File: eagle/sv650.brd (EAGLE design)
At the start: 54.2 x 52.1 mm, 21 parts, among them IC1 7805

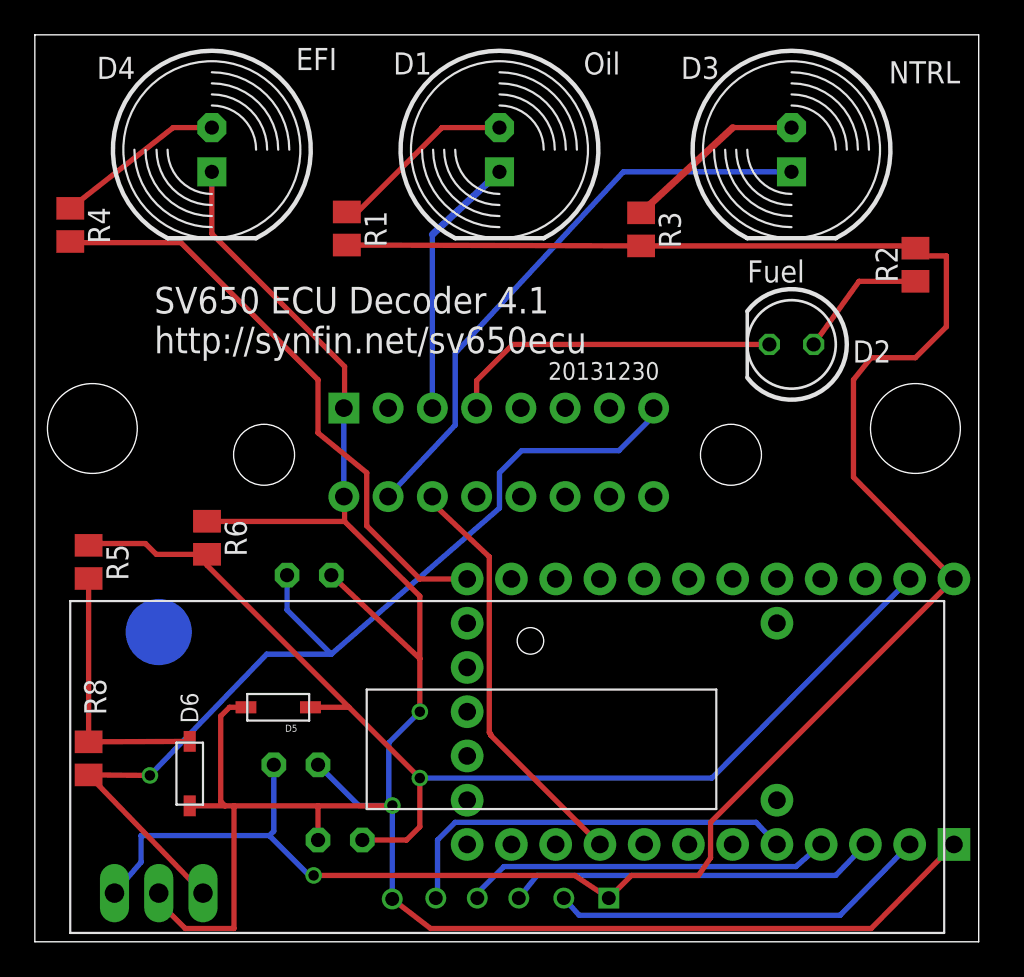
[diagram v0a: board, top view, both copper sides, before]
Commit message: modify the position of parts & traces to be a little cleaner move LED's away from the top edge of the board
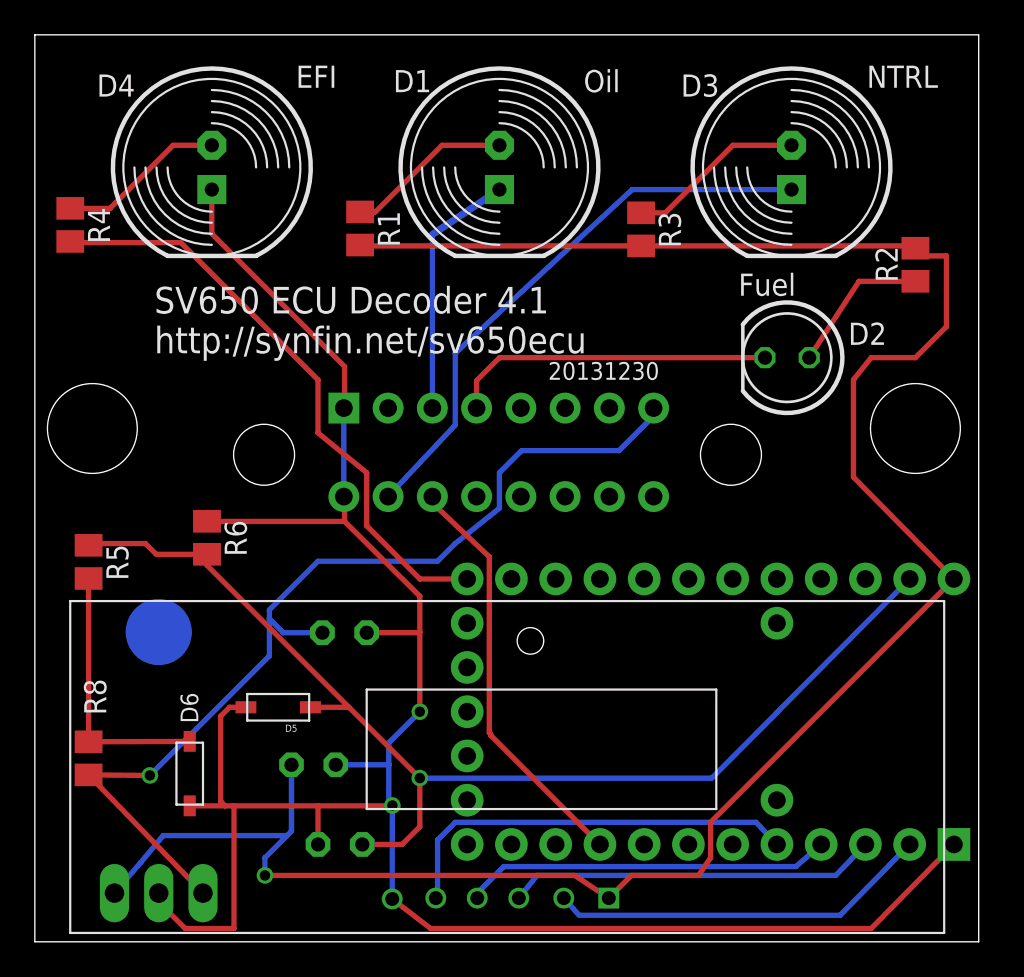
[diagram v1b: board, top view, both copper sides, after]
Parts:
- moved C1 3.88 mm to (17.8, 17.7)
- moved C2 1.02 mm to (16.0, 10.2)
- moved D1 1.02 mm to (26.7, 44.5)
- moved D3 1.02 mm to (43.4, 44.5)
- moved D4 1.02 mm to (10.2, 44.5)
- moved D2 0.80 mm to (43.2, 33.5)
- moved R1 0.76 mm to (18.7, 40.9)
- moved C3 0.25 mm to (17.5, 5.59)
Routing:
- net GND: track 135.6 -> 128.8 mm
- net 5V: track 125.5 -> 127.1 mm
- net N$8: track 10.8 -> 9.73 mm
- net NTRL: track 33.6 -> 32.7 mm
- net N$7: track 7.70 -> 8.47 mm
- net OIL: track 15.2 -> 14.6 mm
- net FUEL: track 19.2 -> 18.7 mm
- net +12V: track 57.4 -> 56.9 mm

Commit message: remove 20V zener replace 5V zener with 4.7V zener (hard to find 5V zeners) merge 10K + 22K into a single 30K resistor clean up traces & remove lots of vias
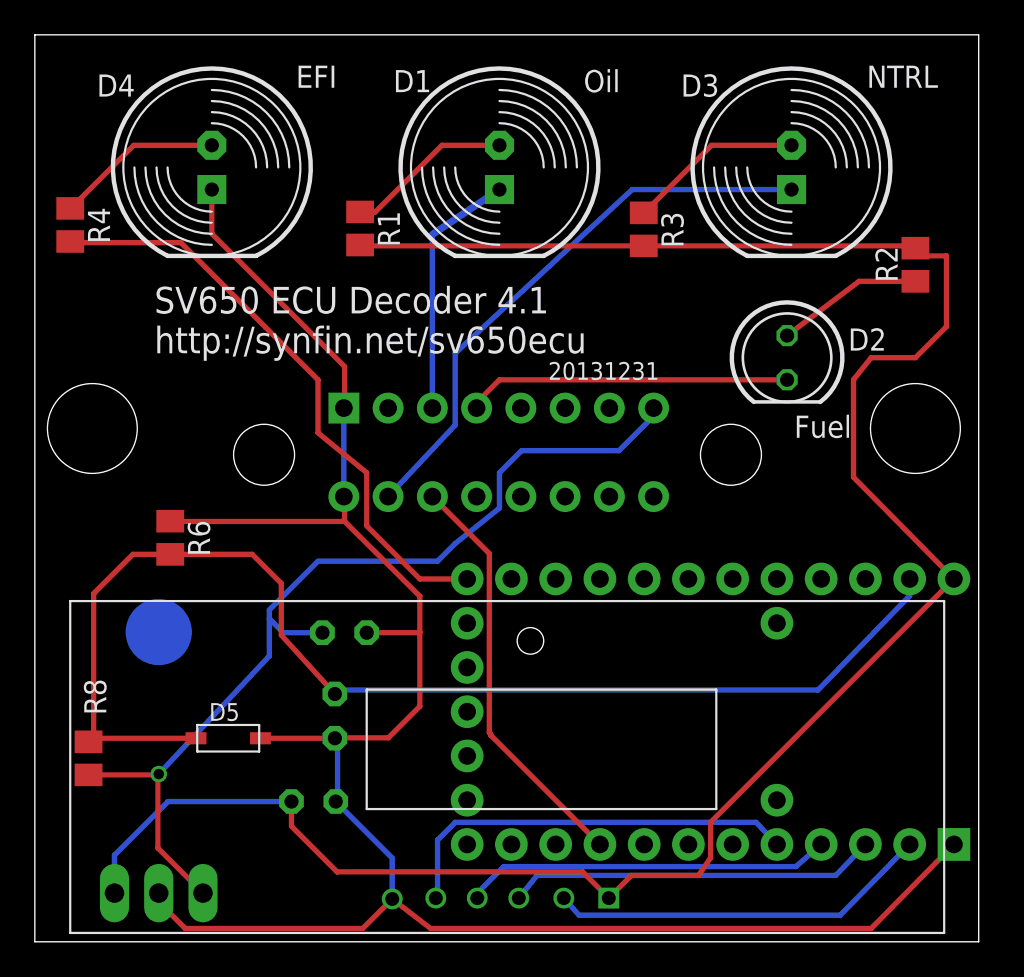
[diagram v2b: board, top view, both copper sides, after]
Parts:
- removed D6: 20V zener, adafruit:SOD-123
- removed R5: 22k, resistor:M0805
- D5: value 5V zener -> 4.7V zener
- R8: value 10k -> 30k
- moved C3 7.37 mm to (17.2, 13.0), turned to 270 degrees
- moved D5 3.38 mm to (11.1, 11.7), turned to 0 degrees
- moved C2 2.11 mm to (16.0, 8.05)
- moved R6 2.11 mm to (7.77, 23.2)
- moved R3 0.15 mm to (35.0, 40.9)
- turned D2 to 270 degrees
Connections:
- removed net N$13: D6.C, R5.2, R8.1
- net ADC: now also R8.1; no longer R5.1
- net GND: no longer D6.A
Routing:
- net N$13: track 15.2 -> 0.00 mm
- net GND: track 128.8 -> 118.7 mm, vias 2 -> 0
- net ADC: track 66.8 -> 71.0 mm, vias 1 -> 0
- net 5V: track 127.1 -> 123.5 mm, vias 1 -> 0
- net +12V: track 56.9 -> 55.4 mm
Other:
- board text added: "20131231"
- board text removed: "20131230"

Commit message: Add 'mode' button Add means to detect Very Low Fuel on later models Move +12V back to ignition
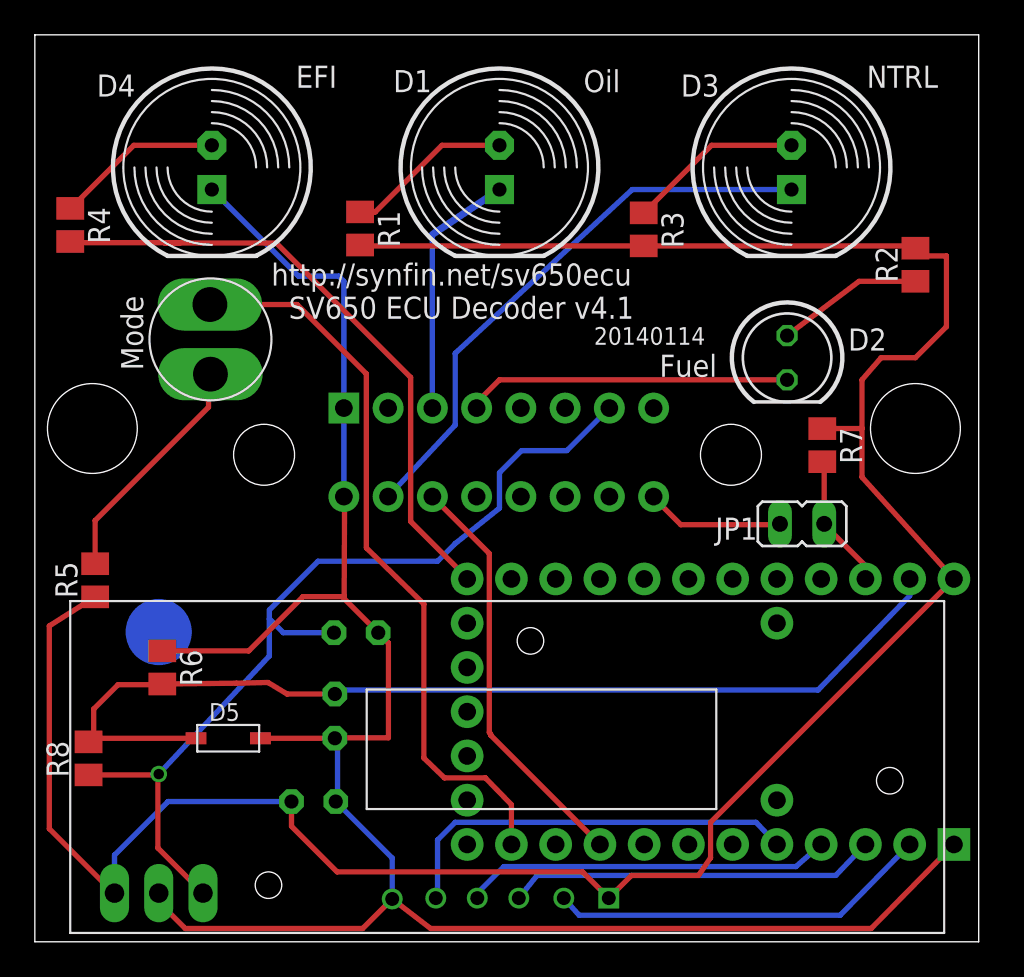
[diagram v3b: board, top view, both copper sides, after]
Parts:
- added JP1: (no value), jumper:JP1
- added R5, R7: 10k, resistor:M0805
- added U$10: R13-509A-05-BB/R13-509A-05-BR, synfinatic:R13-509A-05-BB/R13-509A-05-BR
- added U$2, U$6: (no value), synfinatic:STANDOFF
- moved R6 7.46 mm to (7.32, 15.7)
- moved C1 0.66 mm to (18.4, 17.7)
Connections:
- net ADC renamed BATTMON
- new net FUEL2: JP1.1, R7.2, _1.F1
- new net LOWFUEL2: JP1.2, U$3.P$16
- new net MODE: U$10.P$2, _1.C6
- new net N$12: R5.2, U$10.P$1
- net +12V: now also U$3.P$7; no longer U$3.P$8
- net 5V: now also R5.1, R7.1
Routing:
- net MODE: track 0.00 -> 42.5 mm
- net 5V: track 123.5 -> 144.9 mm
- net N$12: track 0.00 -> 14.1 mm
- net BATTMON: track 71.0 -> 59.0 mm
- net LOWFUEL2: track 0.00 -> 7.97 mm
- net FUEL2: track 0.00 -> 7.76 mm
- net N$9: track 34.2 -> 36.6 mm
- net +12V: track 55.4 -> 53.3 mm
- net GND: track 118.7 -> 117.2 mm
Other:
- board text added: "20140114"
- board text added: "Mode"
- board text added: "http://synfin.net/sv650ecu SV650 ECU Decoder v4.1"
- board text removed: "20131231"
- board text removed: "SV650 ECU Decoder 4.1 http://synfin.net/sv650ecu"

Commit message: Update to v4.2. - Move via away from LM7805 to prevent shorting - Increase size of S/N space
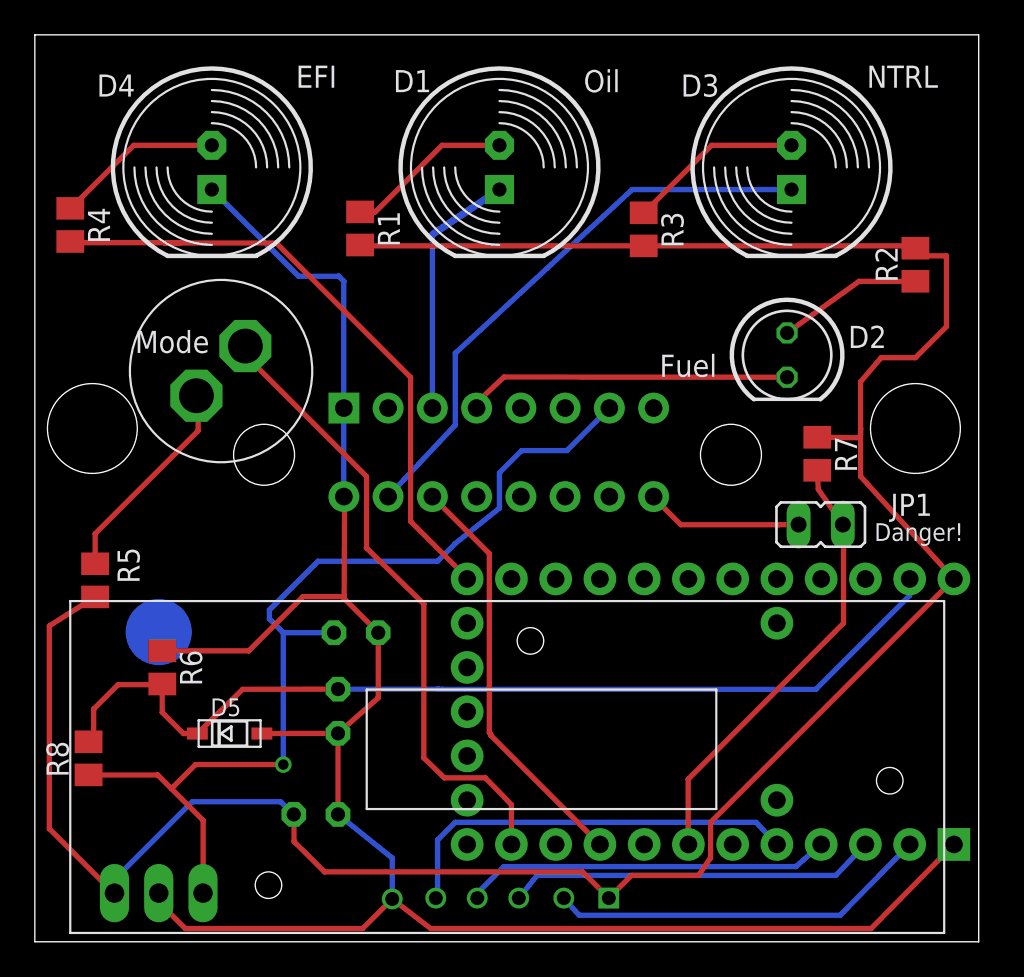
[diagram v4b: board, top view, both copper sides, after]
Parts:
- JP1: value (none) -> (none)
- _1: value TEENSY -> IC2
- moved U$10 1.92 mm to (10.7, 32.8), turned to 45 degrees
- moved JP1 1.07 mm to (45.1, 23.9)
- moved C2 0.75 mm to (16.1, 7.31)
- moved R7 0.58 mm to (44.9, 28.0)
- moved C3 0.33 mm to (17.4, 13.2)
- moved D5 0.28 mm to (11.2, 12.0)
- moved D2 0.15 mm to (43.2, 33.7)
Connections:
- net FUEL2: now also _1.D0; no longer _1.F1
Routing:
- net FUEL2: track 7.76 -> 25.7 mm
- net MODE: track 42.5 -> 36.3 mm
- net +12V: track 53.3 -> 56.3 mm
- net BATTMON: track 59.0 -> 56.2 mm
- net GND: track 117.2 -> 114.8 mm
- net N$12: track 14.1 -> 12.1 mm
- net LOWFUEL2: track 7.97 -> 9.02 mm
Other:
- board text added: "20140309"
- board text added: "CONN1"
- board text added: "Danger!"
- board text added: "http://synfin.net/sv650ecu SV650 ECU Decoder v4.2"
- board text removed: "20140114"
- board text removed: "http://synfin.net/sv650ecu SV650 ECU Decoder v4.1"

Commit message: change mode button to pin D1/6 so we can assign an interrupt to it
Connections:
- net MODE: now also _1.D1; no longer _1.C6
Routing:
- net MODE: track 36.3 -> 44.8 mm, vias 0 -> 2
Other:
- board text added: "20140310"
- board text removed: "20140309"
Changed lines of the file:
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@@
 <text x="47.752" y="49.022" size="1.27" layer="112">NTRL</text>
 <text x="35.8564" y="32.4306" size="1.27" layer="112">Fuel</text>
-<text x="40.624" y="46.558" size="1.016" layer="22" rot="MR0">20140309</text>
+<text x="40.624" y="46.558" size="1.016" layer="22" rot="MR0">20140310</text>
 <rectangle x1="45.638" y1="32.582" x2="51.734" y2="51.568" layer="22"/>
 <text x="5.75" y="33.8" size="1.27" layer="25">Mode</text>
@@
 <signal name="MODE">
 <contactref element="U$10" pad="P$2"/>
-<contactref element="_1" pad="C6"/>
-<wire x1="27.3558" y1="5.588" x2="27.3558" y2="7.8742" width="0.3048" layer="1"/>
-<wire x1="27.3558" y1="7.8742" x2="25.86" y2="9.41" width="0.3048" layer="1"/>
-<wire x1="25.86" y1="9.41" x2="23.51" y2="9.41" width="0.3048" layer="1"/>
-<wire x1="23.51" y1="9.41" x2="22.33" y2="10.55" width="0.3048" layer="1"/>
-<wire x1="22.33" y1="10.55" x2="22.33" y2="19.39" width="0.3048" layer="1"/>
-<wire x1="22.33" y1="19.39" x2="19.03" y2="22.61" width="0.3048" layer="1"/>
+<wire x1="21.61" y1="19.35" x2="19.03" y2="22.61" width="0.3048" layer="1"/>
 <wire x1="12.083" y1="34.195425" x2="12.083" y2="33.667" width="0.3048" layer="1"/>
 <wire x1="12.083" y1="33.667" x2="19.04" y2="26.71" width="0.3048" layer="1"/>
 <wire x1="19.04" y1="26.71" x2="19.04" y2="22.62" width="0.3048" layer="1"/>
 <wire x1="19.04" y1="22.62" x2="19.03" y2="22.61" width="0.3048" layer="1"/>
+<contactref element="_1" pad="D1"/>
+<wire x1="21.61" y1="19.35" x2="21.64" y2="9.62" width="0.3048" layer="1"/>
+<wire x1="21.64" y1="9.62" x2="21.65" y2="9.39" width="0.3048" layer="1"/>
+<via x="21.65" y="9.39" extent="1-16" drill="0.6"/>
+<wire x1="21.65" y1="9.39" x2="33.4638" y2="9.39" width="0.3048" layer="16"/>
+<via x="33.4638" y="9.39" extent="1-16" drill="0.6"/>
+<wire x1="33.4638" y1="9.39" x2="34.9758" y2="7.878" width="0.3048" layer="1"/>
+<wire x1="34.9758" y1="7.878" x2="34.9758" y2="5.588" width="0.3048" layer="1"/>
 </signal>
 <signal name="FUEL2">

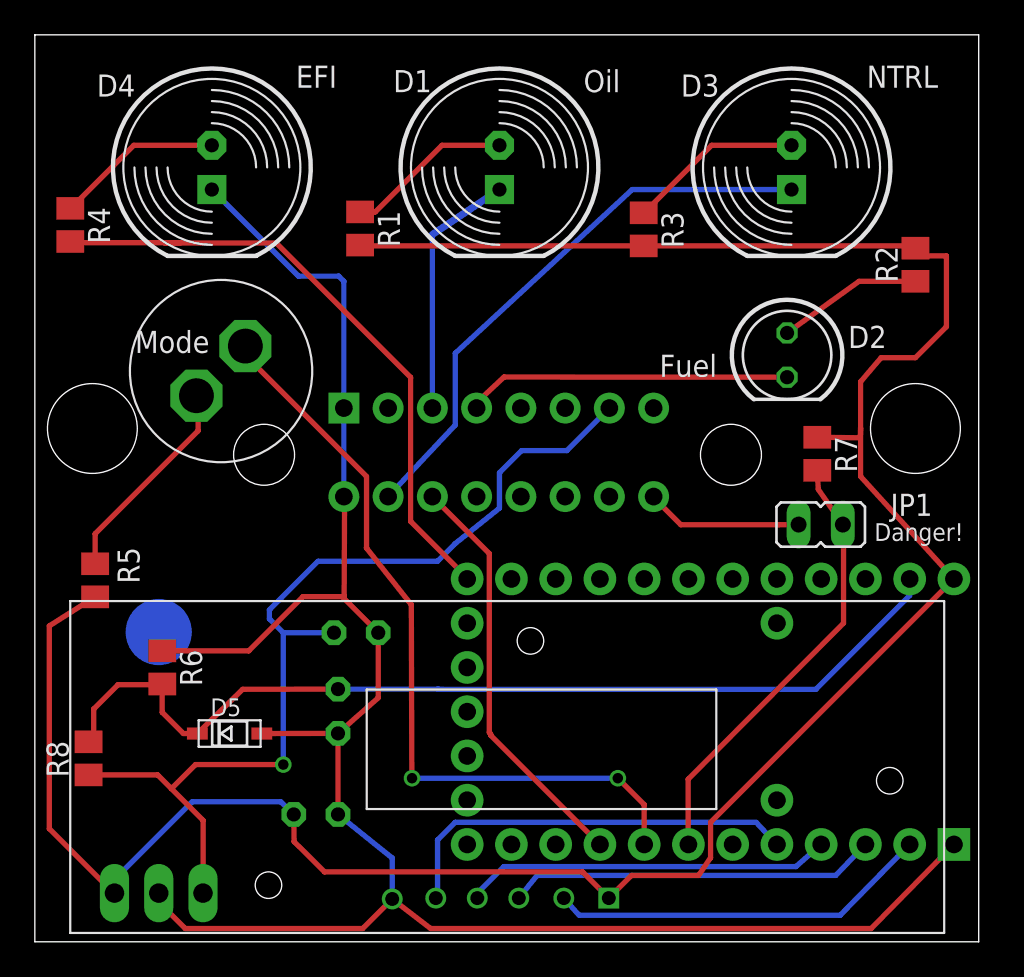
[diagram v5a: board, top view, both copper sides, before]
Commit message: - update board to v4.2 with LM7805 w/ heat sink - fix mode button to use a pin supporting interrupts - remove external pullup resistors
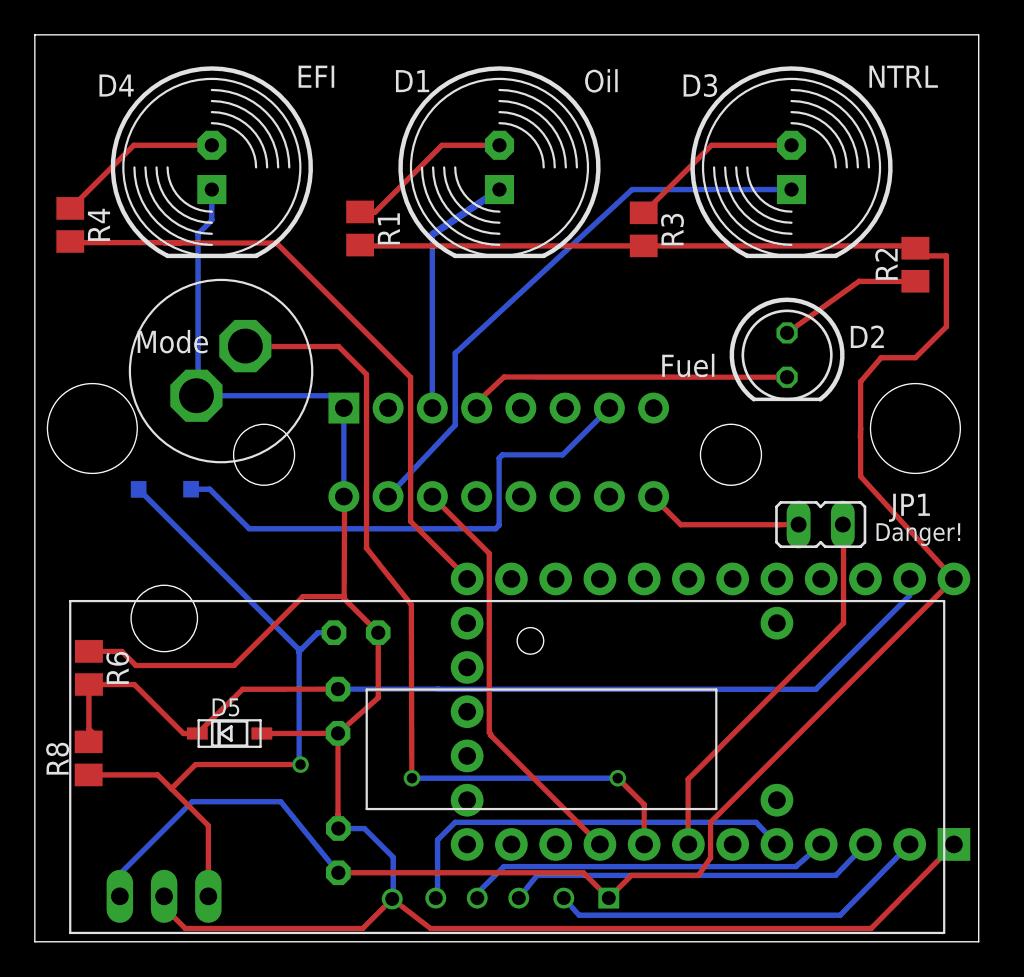
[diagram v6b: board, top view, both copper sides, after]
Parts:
- removed IC1: 7805, linear:TO22H-2
- removed R5, R7: 10k, resistor:M0805
- removed U$2, U$6: (no value), synfinatic:STANDOFF
- added D6: 20V schottky, synfinatic:SOD-123
- added IC2: LM7805, synfinatic:TO220-SINK
- moved R6 4.21 mm to (3.11, 15.7)
- moved C2 2.45 mm to (17.4, 5.23), turned to 90 degrees
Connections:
- net +12V: now also D6.C, IC2.IN; no longer IC1.1, U$3.P$7
- net 5V: now also IC2.OUT; no longer IC1.3, R5.1, R7.1
- net FUEL2: no longer R7.2
- net GND: now also IC2.GND, U$10.P$1; no longer IC1.2
- net N$12: now also D6.A, U$3.P$7; no longer R5.2, U$10.P$1
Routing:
- net 5V: track 145.0 -> 121.9 mm
- net N$12: track 12.1 -> 30.1 mm
- net +12V: track 56.3 -> 42.3 mm
- net GND: track 114.8 -> 124.0 mm
- net FUEL2: track 25.7 -> 22.1 mm
- net MODE: track 44.8 -> 48.0 mm
